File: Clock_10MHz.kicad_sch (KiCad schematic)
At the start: 11 parts, among them U3 74LV8154, U4 74LS151, X1 ASCO

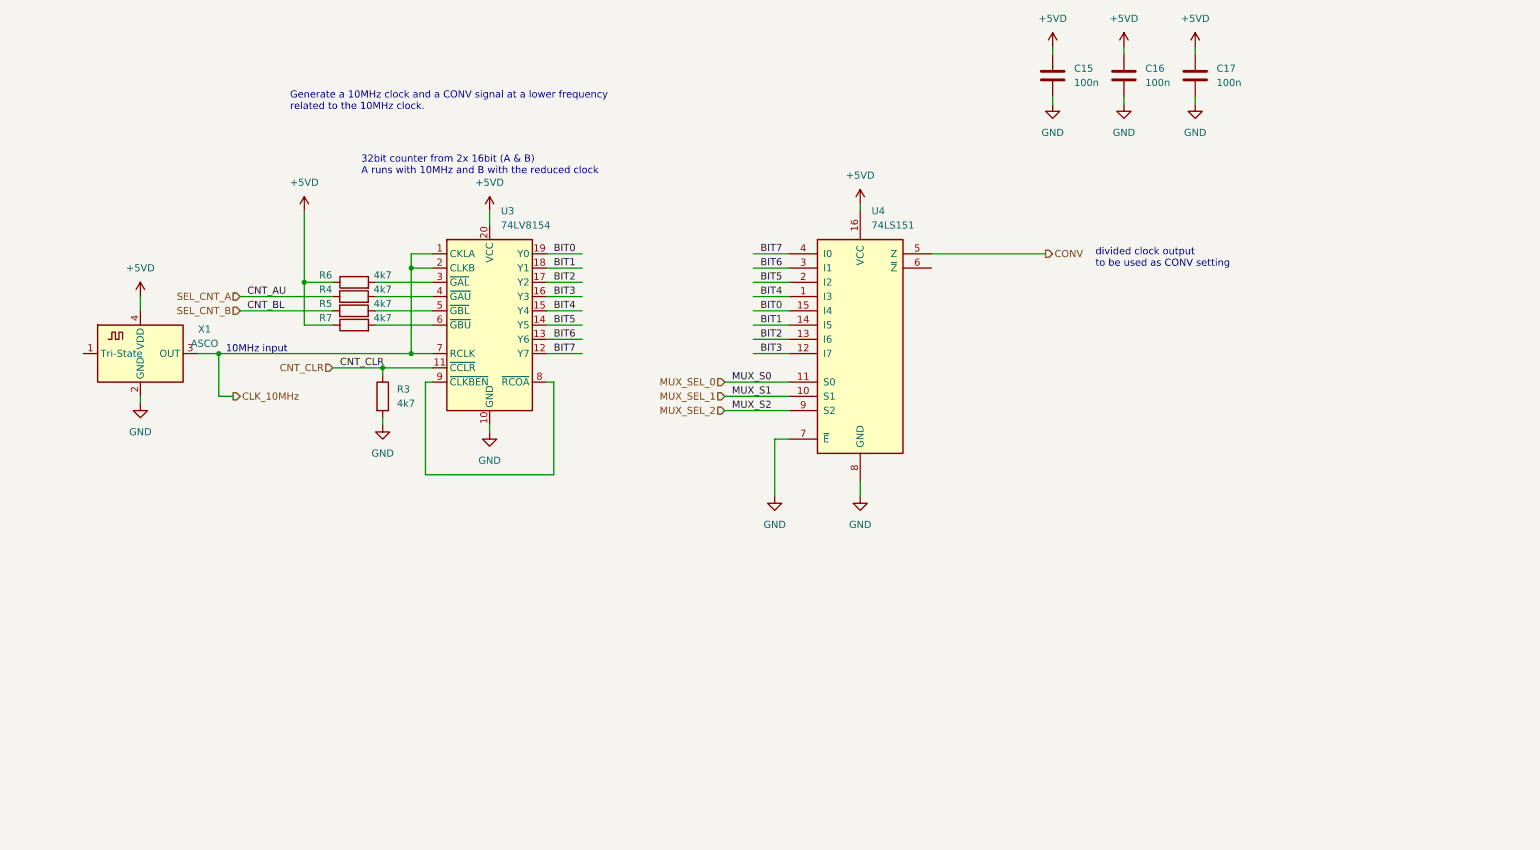
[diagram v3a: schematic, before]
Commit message: changed setting of clock divider to I2C
reduces pin load on uC, thus frees pins for usage with other functions.
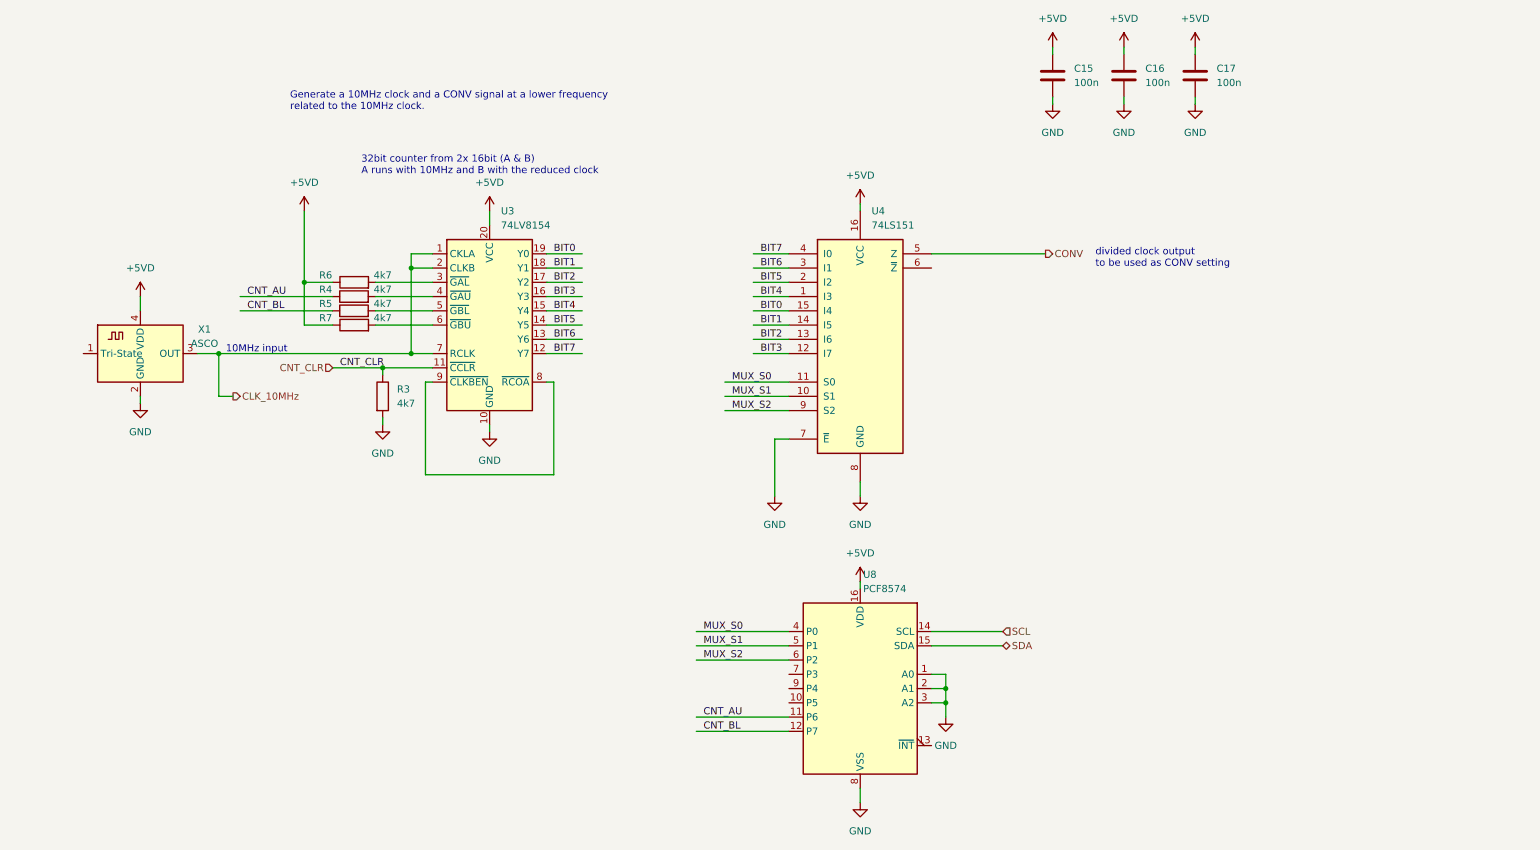
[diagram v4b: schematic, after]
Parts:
- added U8: PCF8574, Package_SO:SOIC-16W_7.5x10.3mm_P1.27mm, symbol Interface_Expansion:PCF8574
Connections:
- net +5VD: now also U8.16 (VDD)
- net GND: now also U8.1 (A0), U8.2 (A1), U8.3 (A2), U8.8 (VSS)
- net MUX_SEL_0 renamed MUX_S0
- net MUX_S0: now also U8.4 (P0)
- net MUX_SEL_1 renamed MUX_S1
- net MUX_S1: now also U8.5 (P1)
- net MUX_SEL_2 renamed MUX_S2
- net MUX_S2: now also U8.6 (P2)
- net SEL_CNT_A renamed CNT_AU
- net SEL_CNT_B renamed CNT_BL
- new net SCL: U8.14 (SCL)
- new net SDA: U8.15 (SDA)
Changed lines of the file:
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@@
   (junction (at 80.01 92.71) (diameter 0) (color 0 0 0 0)
   )
+  (junction (at 180.34 149.86) (diameter 0) (color 0 0 0 0)
+  )
   (junction (at 66.04 77.47) (diameter 0) (color 0 0 0 0)
   )
   (junction (at 50.8 90.17) (diameter 0) (color 0 0 0 0)
   )
+  (junction (at 180.34 152.4) (diameter 0) (color 0 0 0 0)
+  )
   (wire (pts (xy 212.09 44.45) (xy 212.09 45.72))
     (stroke (width 0) (type default) (color 0 0 0 0))
   )
+  (wire (pts (xy 135.89 157.48) (xy 152.3621 157.48))
+    (stroke (width 0) (type default) (color 0 0 0 0))
+  )
+  (wire (pts (xy 135.89 142.24) (xy 152.4 142.24))
+    (stroke (width 0) (type default) (color 0 0 0 0))
+  )
   (wire (pts (xy 66.04 64.77) (xy 66.04 77.47))
     (stroke (width 0) (type default) (color 0 0 0 0))
@@
     (stroke (width 0) (type default) (color 0 0 0 0))
   )
+  (wire (pts (xy 165.1 130.81) (xy 165.1 132.08))
+    (stroke (width 0) (type default) (color 0 0 0 0))
+  )
   (wire (pts (xy 36.83 97.79) (xy 36.83 99.06))
     (stroke (width 0) (type default) (color 0 0 0 0))
@@
     (stroke (width 0) (type default) (color 0 0 0 0))
   )
+  (wire (pts (xy 165.1 167.64) (xy 165.1 170.18))
+    (stroke (width 0) (type default) (color 0 0 0 0))
+  )
   (wire (pts (xy 71.12 92.71) (xy 80.01 92.71))
     (stroke (width 0) (type default) (color 0 0 0 0))
@@
     (stroke (width 0) (type default) (color 0 0 0 0))
   )
+  (wire (pts (xy 177.8 142.24) (xy 190.5 142.24))
+    (stroke (width 0) (type default) (color 0 0 0 0))
+  )
   (wire (pts (xy 146.05 82.55) (xy 152.4 82.55))
     (stroke (width 0) (type default) (color 0 0 0 0))
@@
     (stroke (width 0) (type default) (color 0 0 0 0))
   )
+  (wire (pts (xy 177.8 152.4) (xy 180.34 152.4))
+    (stroke (width 0) (type default) (color 0 0 0 0))
+  )
   (wire (pts (xy 149.86 105.41) (xy 149.86 115.57))
     (stroke (width 0) (type default) (color 0 0 0 0))
@@
     (stroke (width 0) (type default) (color 0 0 0 0))
   )
+  (wire (pts (xy 135.89 144.78) (xy 152.4 144.78))
+    (stroke (width 0) (type default) (color 0 0 0 0))
+  )
   (wire (pts (xy 85.09 72.39) (xy 85.09 74.93))
     (stroke (width 0) (type default) (color 0 0 0 0))
@@
     (stroke (width 0) (type default) (color 0 0 0 0))
   )
+  (wire (pts (xy 177.8 149.86) (xy 180.34 149.86))
+    (stroke (width 0) (type default) (color 0 0 0 0))
+  )
   (wire (pts (xy 78.74 77.47) (xy 88.9 77.47))
     (stroke (width 0) (type default) (color 0 0 0 0))
   )
+  (wire (pts (xy 135.89 154.94) (xy 152.3621 154.94))
+    (stroke (width 0) (type default) (color 0 0 0 0))
+  )
   (wire (pts (xy 53.34 97.79) (xy 50.8 97.79))
     (stroke (width 0) (type default) (color 0 0 0 0))
   )
+  (wire (pts (xy 177.8 139.7) (xy 190.5 139.7))
+    (stroke (width 0) (type default) (color 0 0 0 0))
+  )
+  (wire (pts (xy 177.8 147.32) (xy 180.34 147.32))
+    (stroke (width 0) (type default) (color 0 0 0 0))
+  )
+  (wire (pts (xy 180.34 149.86) (xy 180.34 152.4))
+    (stroke (width 0) (type default) (color 0 0 0 0))
+  )
   (wire (pts (xy 140.97 95.25) (xy 152.4 95.25))
     (stroke (width 0) (type default) (color 0 0 0 0))
@@
     (stroke (width 0) (type default) (color 0 0 0 0))
   )
+  (wire (pts (xy 135.89 139.7) (xy 152.4 139.7))
+    (stroke (width 0) (type default) (color 0 0 0 0))
+  )
   (wire (pts (xy 224.79 44.45) (xy 224.79 45.72))
     (stroke (width 0) (type default) (color 0 0 0 0))
@@
     (stroke (width 0) (type default) (color 0 0 0 0))
   )
+  (wire (pts (xy 180.34 152.4) (xy 180.34 154.94))
+    (stroke (width 0) (type default) (color 0 0 0 0))
+  )
   (wire (pts (xy 36.83 80.01) (xy 36.83 82.55))
     (stroke (width 0) (type default) (color 0 0 0 0))
@@
   )
   (wire (pts (xy 146.05 74.93) (xy 152.4 74.93))
+    (stroke (width 0) (type default) (color 0 0 0 0))
+  )
+  (wire (pts (xy 180.34 147.32) (xy 180.34 149.86))
     (stroke (width 0) (type default) (color 0 0 0 0))
   )
@@
     (effects (font (size 1.27 1.27)) (justify left bottom))
   )
+  (label "CNT_AU" (at 137.16 154.94 0)
+    (effects (font (size 1.27 1.27)) (justify left bottom))
+  )
+  (label "MUX_S2" (at 137.16 144.78 0)
+    (effects (font (size 1.27 1.27)) (justify left bottom))
+  )
+  (label "MUX_S1" (at 137.16 142.24 0)
+    (effects (font (size 1.27 1.27)) (justify left bottom))
+  )
   (label "BIT2" (at 147.32 87.63 0)
     (effects (font (size 1.27 1.27)) (justify left bottom))
@@
     (effects (font (size 1.27 1.27)) (justify left bottom))
   )
+  (label "MUX_S0" (at 137.16 139.7 0)
+    (effects (font (size 1.27 1.27)) (justify left bottom))
+  )
   (label "BIT0" (at 147.32 82.55 0)
     (effects (font (size 1.27 1.27)) (justify left bottom))
   )
+  (label "CNT_BL" (at 137.16 157.48 0)
+    (effects (font (size 1.27 1.27)) (justify left bottom))
+  )
   (label "BIT4" (at 147.32 80.01 0)
     (effects (font (size 1.27 1.27)) (justify left bottom))
@@
     (effects (font (size 1.27 1.27)) (justify left bottom))
   )
-  (hierarchical_label "MUX_SEL_0" (shape input) (at 140.97 95.25 180)
-    (effects (font (size 1.27 1.27)) (justify right))
+  (hierarchical_label "SDA" (shape bidirectional) (at 190.5 142.24 0)
+    (effects (font (size 1.27 1.27)) (justify left))
+  )
+  (hierarchical_label "SCL" (shape input) (at 190.5 139.7 0)
+    (effects (font (size 1.27 1.27)) (justify left))
   )
   (hierarchical_label "CNT_CLR" (shape input) (at 71.12 92.71 180)
@@
     (effects (font (size 1.27 1.27)) (justify left))
   )
-  (hierarchical_label "SEL_CNT_A" (shape input) (at 54.61 80.01 180)
-    (effects (font (size 1.27 1.27)) (justify right))
-  )
-  (hierarchical_label "MUX_SEL_2" (shape input) (at 140.97 100.33 180)
-    (effects (font (size 1.27 1.27)) (justify right))
-  )
-  (hierarchical_label "SEL_CNT_B" (shape input) (at 54.61 82.55 180)
-    (effects (font (size 1.27 1.27)) (justify right))
-  )
-  (hierarchical_label "MUX_SEL_1" (shape input) (at 140.97 97.79 180)
-    (effects (font (size 1.27 1.27)) (justify right))
-  )
   (symbol (lib_id "power:+5VD") (at 212.09 35.56 0) (unit 1)
     (in_bom yes) (on_board yes) (fields_autoplaced)
@@
     )
     (property "Datasheet" "" (id 3) (at 212.09 35.56 0)
+      (effects (font (size 1.27 1.27)) hide)
+    )
+    (pin "1")
+  )
+  (symbol (lib_id "power:GND") (at 165.1 170.18 0) (unit 1)
+    (in_bom yes) (on_board yes) (fields_autoplaced)
+    (property "Reference" "#PWR037" (id 0) (at 165.1 176.53 0)
+      (effects (font (size 1.27 1.27)) hide)
+    )
+    (property "Value" "GND" (id 1) (at 165.1 175.26 0))
+    (property "Footprint" "" (id 2) (at 165.1 170.18 0)
+      (effects (font (size 1.27 1.27)) hide)
+    )
+    (property "Datasheet" "" (id 3) (at 165.1 170.18 0)
       (effects (font (size 1.27 1.27)) hide)
     )
@@
     (pin "1")
     (pin "2")
+  )
+  (symbol (lib_id "power:+5VD") (at 165.1 130.81 0) (unit 1)
+    (in_bom yes) (on_board yes) (fields_autoplaced)
+    (property "Reference" "#PWR036" (id 0) (at 165.1 134.62 0)
+      (effects (font (size 1.27 1.27)) hide)
+    )
+    (property "Value" "+5VD" (id 1) (at 165.1 125.73 0))
+    (property "Footprint" "" (id 2) (at 165.1 130.81 0)
+      (effects (font (size 1.27 1.27)) hide)
+    )
+    (property "Datasheet" "" (id 3) (at 165.1 130.81 0)
+      (effects (font (size 1.27 1.27)) hide)
+    )
+    (pin "1")
   )
   (symbol (lib_id "power:GND") (at 199.39 45.72 0) (unit 1)
@@
     (pin "9")
   )
+  (symbol (lib_id "power:GND") (at 180.34 154.94 0) (unit 1)
+    (in_bom yes) (on_board yes) (fields_autoplaced)
+    (property "Reference" "#PWR038" (id 0) (at 180.34 161.29 0)
+      (effects (font (size 1.27 1.27)) hide)
+    )
+    (property "Value" "GND" (id 1) (at 180.34 160.02 0))
+    (property "Footprint" "" (id 2) (at 180.34 154.94 0)
+      (effects (font (size 1.27 1.27)) hide)
+    )
+    (property "Datasheet" "" (id 3) (at 180.34 154.94 0)
+      (effects (font (size 1.27 1.27)) hide)
+    )
+    (pin "1")
+  )
   (symbol (lib_id "Device:R") (at 80.01 97.79 0) (unit 1)
     (in_bom yes) (on_board yes) (fields_autoplaced)
@@
     (pin "1")
   )
+  (symbol (lib_id "Interface_Expansion:PCF8574") (at 165.1 149.86 0) (mirror y) (unit 1)
+    (in_bom yes) (on_board yes) (fields_autoplaced)
+    (property "Reference" "U8" (id 0) (at 165.6206 129.54 0)
+      (effects (font (size 1.27 1.27)) (justify right))
+    )
+    (property "Value" "PCF8574" (id 1) (at 165.6206 132.08 0)
+      (effects (font (size 1.27 1.27)) (justify right))
+    )
+    (property "Footprint" "Package_SO:SOIC-16W_7.5x10.3mm_P1.27mm" (id 2) (at 165.1 149.86 0)
+      (effects (font (size 1.27 1.27)) hide)
+    )
+    (property "Datasheet" "http://www.nxp.com/documents/data_sheet/PCF8574_PCF8574A.pdf" (id 3) (at 165.1 149.86 0)
+      (effects (font (size 1.27 1.27)) hide)
+    )
+    (pin "1")
+    (pin "10")
+    (pin "11")
+    (pin "12")
+    (pin "13")
+    (pin "14")
+    (pin "15")
+    (pin "16")
+    (pin "2")
+    (pin "3")
+    (pin "4")
+    (pin "5")
+    (pin "6")
+    (pin "7")
+    (pin "8")
+    (pin "9")
+  )
   (symbol (lib_id "power:+5VD") (at 99.06 64.77 0) (unit 1)

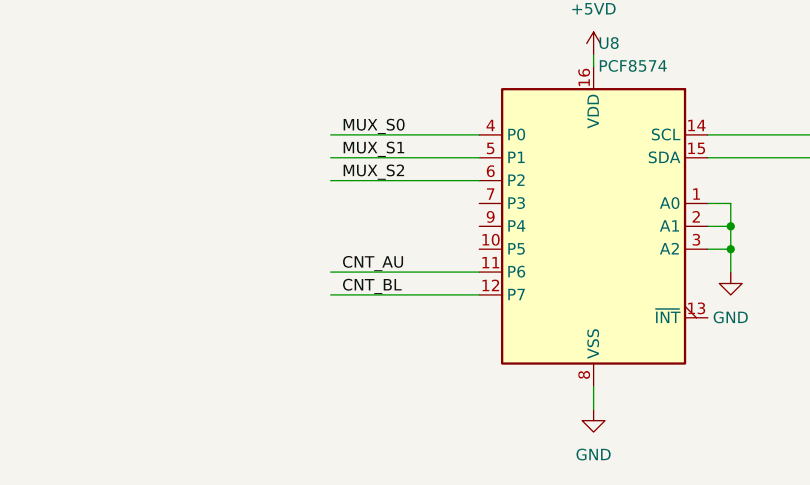
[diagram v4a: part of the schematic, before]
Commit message: implemented linear regulators
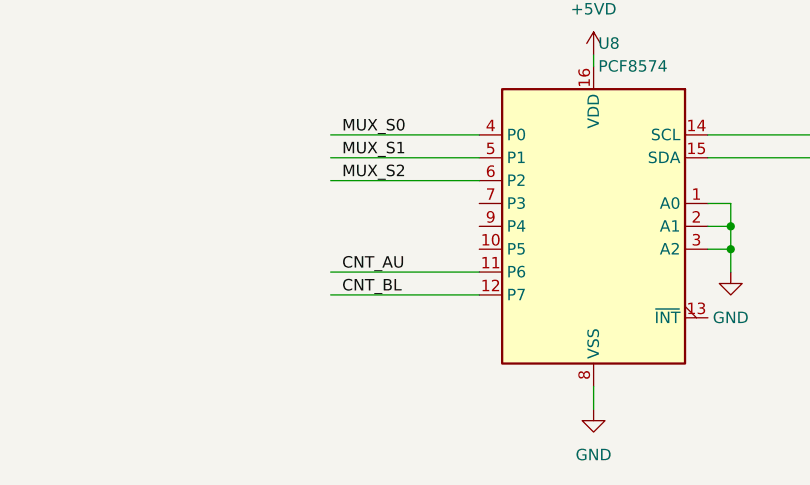
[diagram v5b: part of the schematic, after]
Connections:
- net CNT_AU: now also U8.11 (P6)
- net CNT_BL: now also U8.12 (P7)
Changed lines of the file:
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@@
     (stroke (width 0) (type default) (color 0 0 0 0))
   )
-  (wire (pts (xy 135.89 157.48) (xy 152.3621 157.48))
+  (wire (pts (xy 135.89 157.48) (xy 152.4 157.48))
     (stroke (width 0) (type default) (color 0 0 0 0))
   )
@@
     (stroke (width 0) (type default) (color 0 0 0 0))
   )
-  (wire (pts (xy 135.89 154.94) (xy 152.3621 154.94))
+  (wire (pts (xy 135.89 154.94) (xy 152.4 154.94))
     (stroke (width 0) (type default) (color 0 0 0 0))
   )
